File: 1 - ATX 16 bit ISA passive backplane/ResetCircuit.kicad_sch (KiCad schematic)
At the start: 32 parts

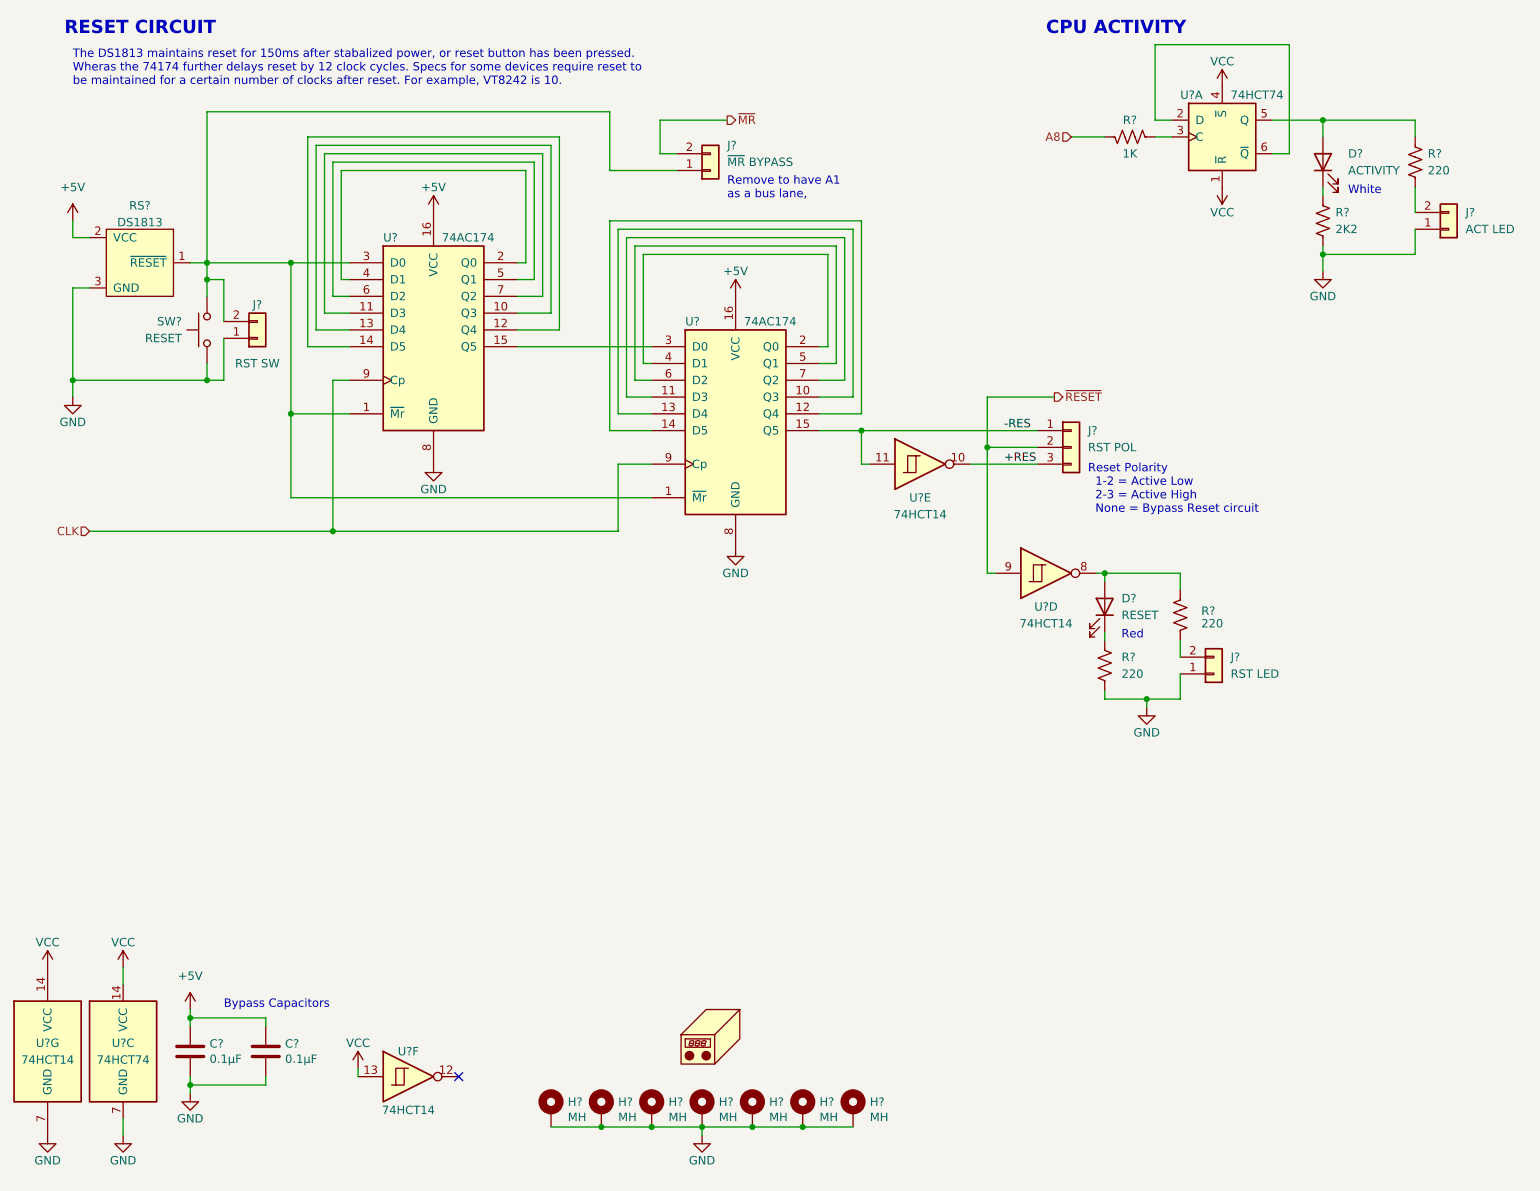
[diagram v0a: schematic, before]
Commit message: Removed unessential components and added capacitors on the bus lanes. Still need work for on the silkscreen side.
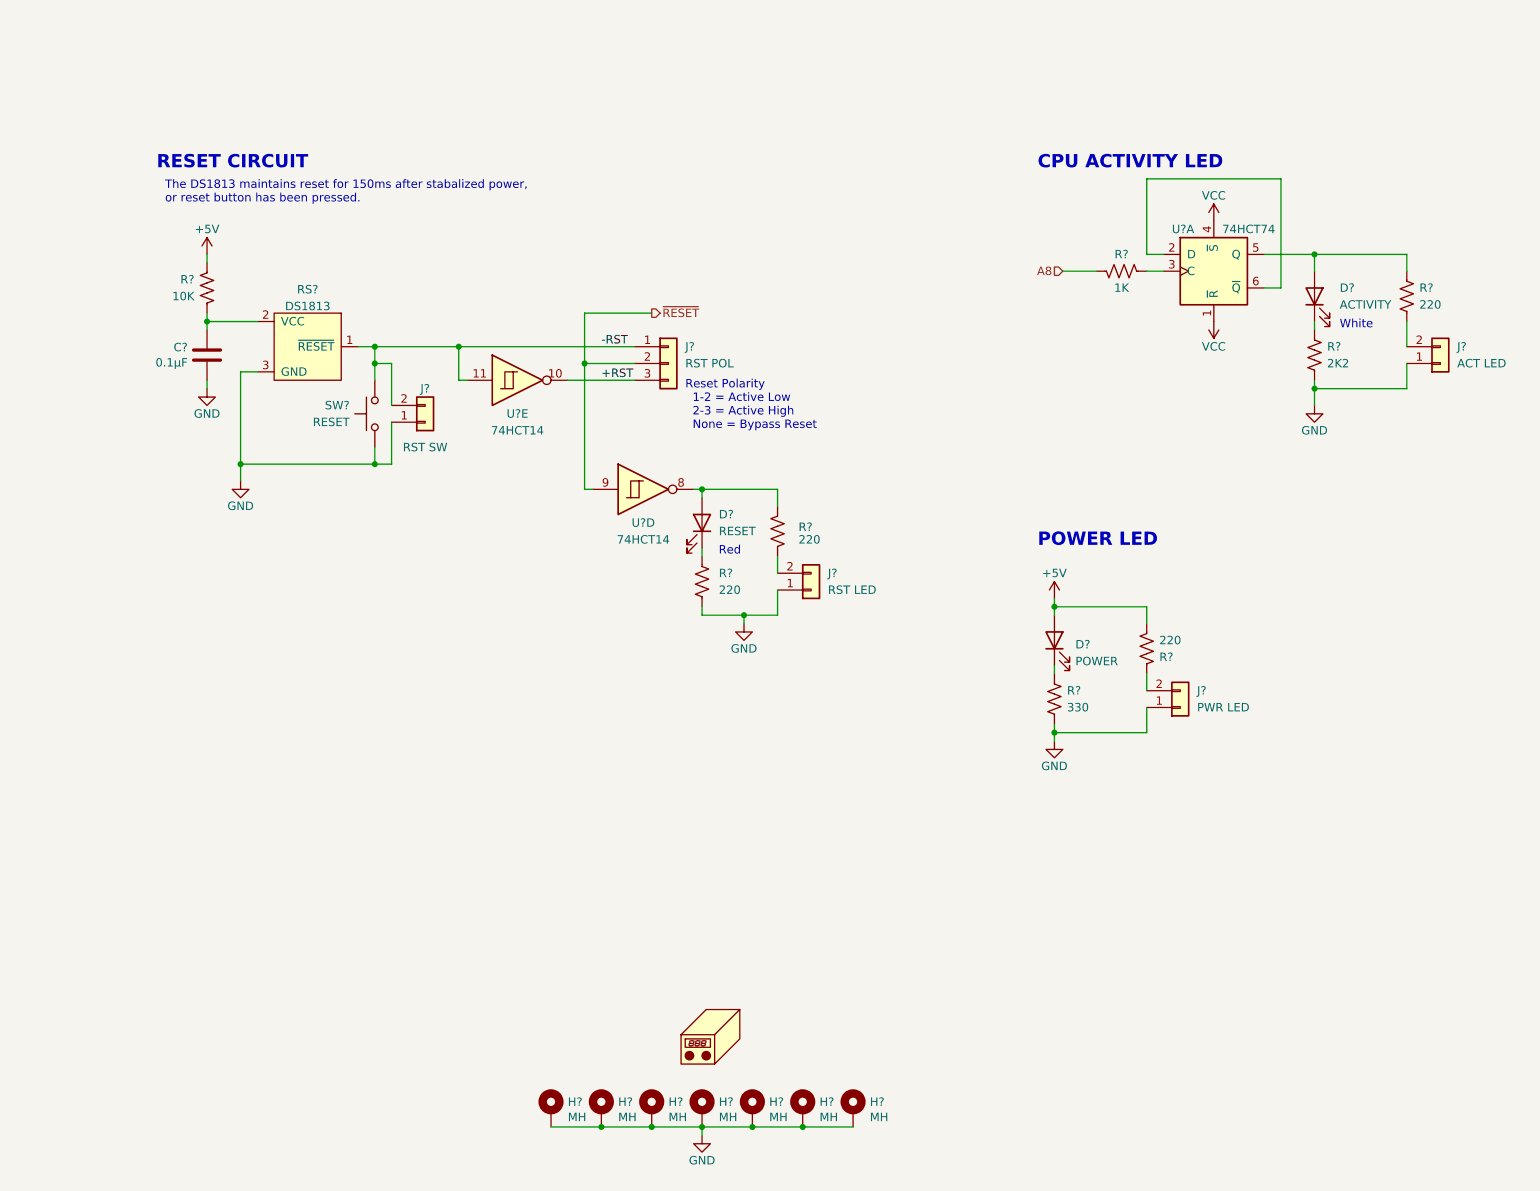
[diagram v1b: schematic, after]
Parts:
- removed C? (x2): 0.1µF, Capacitor_THT:C_Disc_D3.0mm_W1.6mm_P2.50mm, symbol Device:C
- removed J?: ~{MR} BYPASS, Connector_PinHeader_2.54mm:PinHeader_1x02_P2.54mm_Vertical, symbol Connector_Generic:Conn_01x02
- removed U? (x2): 74AC174, Package_DIP:DIP-16_W7.62mm, symbol 74xx:74LS174
- removed U?: 74HCT74, Package_DIP:DIP-14_W7.62mm, symbol 74xx:74HC74
- removed U? (x2): 74HCT14, Package_DIP:DIP-14_W7.62mm, symbol 74xx:74HC14
- added C?: 0.1µF, Capacitor_THT:C_Disc_D3.0mm_W1.6mm_P2.50mm, symbol Device:C
- added D?: POWER, LED_THT:LED_D3.0mm, symbol Device:LED
- added J?: PWR LED, 0 - Library:PinHeader_1x2_Vertical (Modified), symbol Connector_Generic:Conn_01x02
- added R?: 220, Resistor_THT:R_Axial_DIN0207_L6.3mm_D2.5mm_P10.16mm_Horizontal, symbol Device:R_US
- added R?: 330, Resistor_THT:R_Axial_DIN0207_L6.3mm_D2.5mm_P10.16mm_Horizontal, symbol Device:R_US
- added R?: 10K, Resistor_THT:R_Axial_DIN0207_L6.3mm_D2.5mm_P10.16mm_Horizontal, symbol Device:R_US
- J? (x3): footprint Connector_PinHeader_2.54mm:PinHeader_1x02_P2.54mm_Vertical -> 0 - Library:PinHeader_1x2_Vertical (Modified)
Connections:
- net -RES is gone; now on net -RST: J?.1 (Pin_1), U?.11
- net +5V: now also D?.2 (A), R?.1, R?.2; no longer RS?.2 (VCC)
- net GND: now also C?.2, J?.1 (Pin_1), R?.2
- net -RST: now reaches J?.2 (Pin_2), RS?.1 (~{RESET}), SW?.1
- net +RES renamed +RST
- new net: D?.1 (K), R?.1
- new net: J?.2 (Pin_2), R?.1
- new net: C?.1, R?.2, RS?.2 (VCC)
- no-connect marks 1 -> 0
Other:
- note added: "CPU ACTIVITY LED"
- note added: "POWER LED"
- note added: "Reset Polarity 1-2 = Active Low 2-3 = Active High None = Bypass Reset"
- note added: "The DS1813 maintains reset for 150ms after stabalized power, or reset button has been pressed."
- note removed: "Bypass Capacitors"
- note removed: "CPU ACTIVITY"
- note removed: "Remove to have A1 as a bus lane,"
- note removed: "Reset Polarity 1-2 = Active Low 2-3 = Active High None = Bypass Reset circuit"
- note removed: "The DS1813 maintains reset for 150ms after stabalized power, or reset button has been pressed. Wheras the 74174 further delays reset by 12 clock cycles. Specs for some devices require reset to be maintained for a certain number of clocks after reset. For example, VT8242 is 10."
- moved on the sheet: D?, J?, R?, RS?, SW?, U?A, U?D, U?E

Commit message: Minor tweaks to the backplane, and will be sending it out for manufacture
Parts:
- H? (x7): footprint 0 - Library:MountingHole_M3.96_Pad_Via_ATX -> 0_Library:MountingHole_M3.96_Pad_Via_ATX
- J? (x4): footprint 0 - Library:PinHeader_1x2_Vertical (Modified) -> 0_Library:PinHeader_1x2_Vertical (Modified)
- N?: footprint 0 - Library:ATX_Backplane -> 0_Library:ATX_Backplane
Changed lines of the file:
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@@
       (effects (font (size 1.27 1.27)) (justify left))
     )
-    (property "Footprint" "0 - Library:MountingHole_M3.96_Pad_Via_ATX" (at 99.06 189.23 0)
+    (property "Footprint" "0_Library:MountingHole_M3.96_Pad_Via_ATX" (at 99.06 189.23 0)
       (effects (font (size 1.27 1.27)) hide)
     )
@@
       (effects (font (size 1.27 1.27)) (justify left))
     )
-    (property "Footprint" "0 - Library:MountingHole_M3.96_Pad_Via_ATX" (at 121.92 189.23 0)
+    (property "Footprint" "0_Library:MountingHole_M3.96_Pad_Via_ATX" (at 121.92 189.23 0)
       (effects (font (size 1.27 1.27)) hide)
     )
@@
       (effects (font (size 1.27 1.27)) (justify left))
     )
-    (property "Footprint" "0 - Library:PinHeader_1x2_Vertical (Modified)" (at 194.31 128.27 0)
+    (property "Footprint" "0_Library:PinHeader_1x2_Vertical (Modified)" (at 194.31 128.27 0)
       (effects (font (size 1.27 1.27)) hide)
     )
@@
       (effects (font (size 1.27 1.27)) (justify left))
     )
-    (property "Footprint" "0 - Library:MountingHole_M3.96_Pad_Via_ATX" (at 114.3 189.23 0)
+    (property "Footprint" "0_Library:MountingHole_M3.96_Pad_Via_ATX" (at 114.3 189.23 0)
       (effects (font (size 1.27 1.27)) hide)
     )
@@
       (effects (font (size 1.27 1.27)) (justify left))
     )
-    (property "Footprint" "0 - Library:MountingHole_M3.96_Pad_Via_ATX" (at 137.16 189.23 0)
+    (property "Footprint" "0_Library:MountingHole_M3.96_Pad_Via_ATX" (at 137.16 189.23 0)
       (effects (font (size 1.27 1.27)) hide)
     )
@@
       (effects (font (size 1.27 1.27)) (justify left))
     )
-    (property "Footprint" "0 - Library:MountingHole_M3.96_Pad_Via_ATX" (at 129.54 189.23 0)
+    (property "Footprint" "0_Library:MountingHole_M3.96_Pad_Via_ATX" (at 129.54 189.23 0)
       (effects (font (size 1.27 1.27)) hide)
     )
@@
       (effects (font (size 1.27 1.27)) (justify left) hide)
     )
-    (property "Footprint" "0 - Library:ATX_Backplane" (at 125.73 176.53 0)
+    (property "Footprint" "0_Library:ATX_Backplane" (at 125.73 176.53 0)
       (effects (font (size 1.27 1.27)) hide)
     )
@@
       (effects (font (size 1.27 1.27)) (justify left))
     )
-    (property "Footprint" "0 - Library:PinHeader_1x2_Vertical (Modified)" (at 233.68 76.2 0)
+    (property "Footprint" "0_Library:PinHeader_1x2_Vertical (Modified)" (at 233.68 76.2 0)
       (effects (font (size 1.27 1.27)) hide)
     )
@@
       (effects (font (size 1.27 1.27)) (justify left))
     )
-    (property "Footprint" "0 - Library:PinHeader_1x2_Vertical (Modified)" (at 138.43 110.49 0)
+    (property "Footprint" "0_Library:PinHeader_1x2_Vertical (Modified)" (at 138.43 110.49 0)
       (effects (font (size 1.27 1.27)) hide)
     )
@@
       (effects (font (size 1.27 1.27)) (justify left))
     )
-    (property "Footprint" "0 - Library:MountingHole_M3.96_Pad_Via_ATX" (at 144.78 189.23 0)
+    (property "Footprint" "0_Library:MountingHole_M3.96_Pad_Via_ATX" (at 144.78 189.23 0)
       (effects (font (size 1.27 1.27)) hide)
     )
@@
       (effects (font (size 1.27 1.27)))
     )
-    (property "Footprint" "0 - Library:PinHeader_1x2_Vertical (Modified)" (at 80.01 85.09 0)
+    (property "Footprint" "0_Library:PinHeader_1x2_Vertical (Modified)" (at 80.01 85.09 0)
       (effects (font (size 1.27 1.27)) hide)
     )
@@
       (effects (font (size 1.27 1.27)) (justify left))
     )
-    (property "Footprint" "0 - Library:MountingHole_M3.96_Pad_Via_ATX" (at 106.68 189.23 0)
-      (effects (font (size 1.27 1.27)) hide)
-    )
+    (property "Footprint" "0_Library:MountingHole_M3.96_Pad_Via_ATX" (at 106.68 189.23 0)
+      (effects (font (size 1.27 1.27)) hide)
+    )

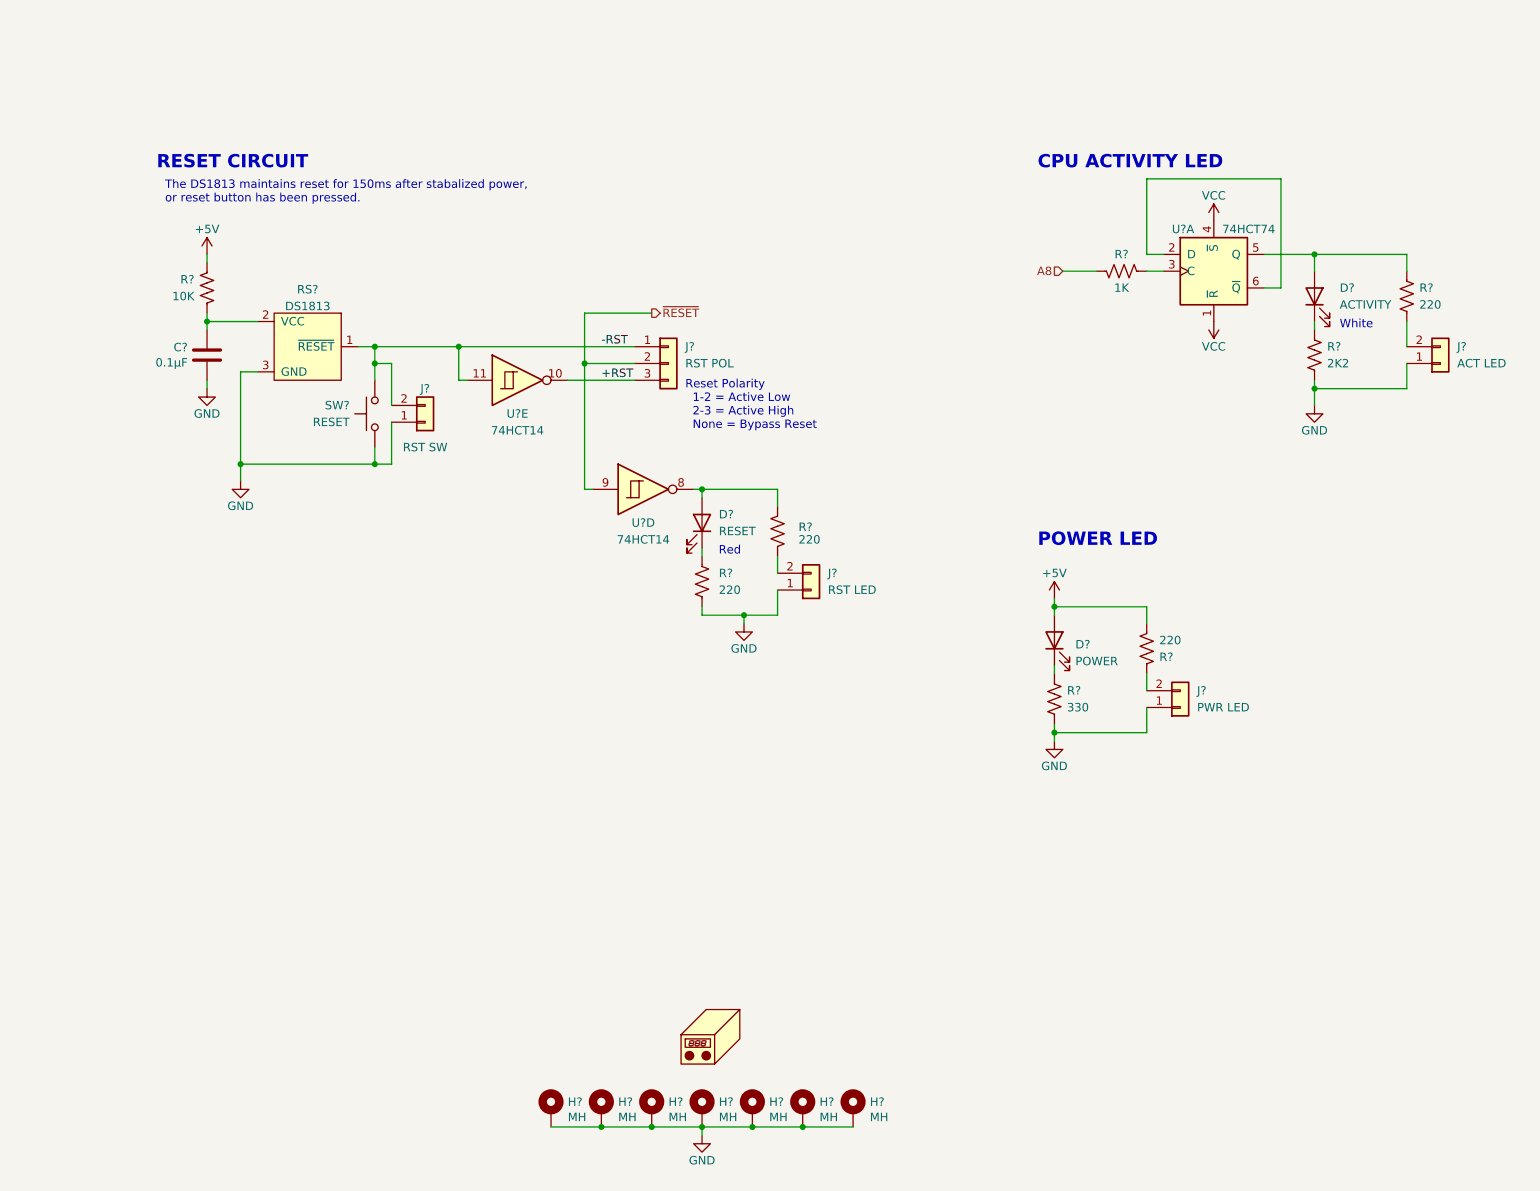
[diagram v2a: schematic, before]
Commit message: Updated disk activity circuit in mother board, and improved layout in CPU card
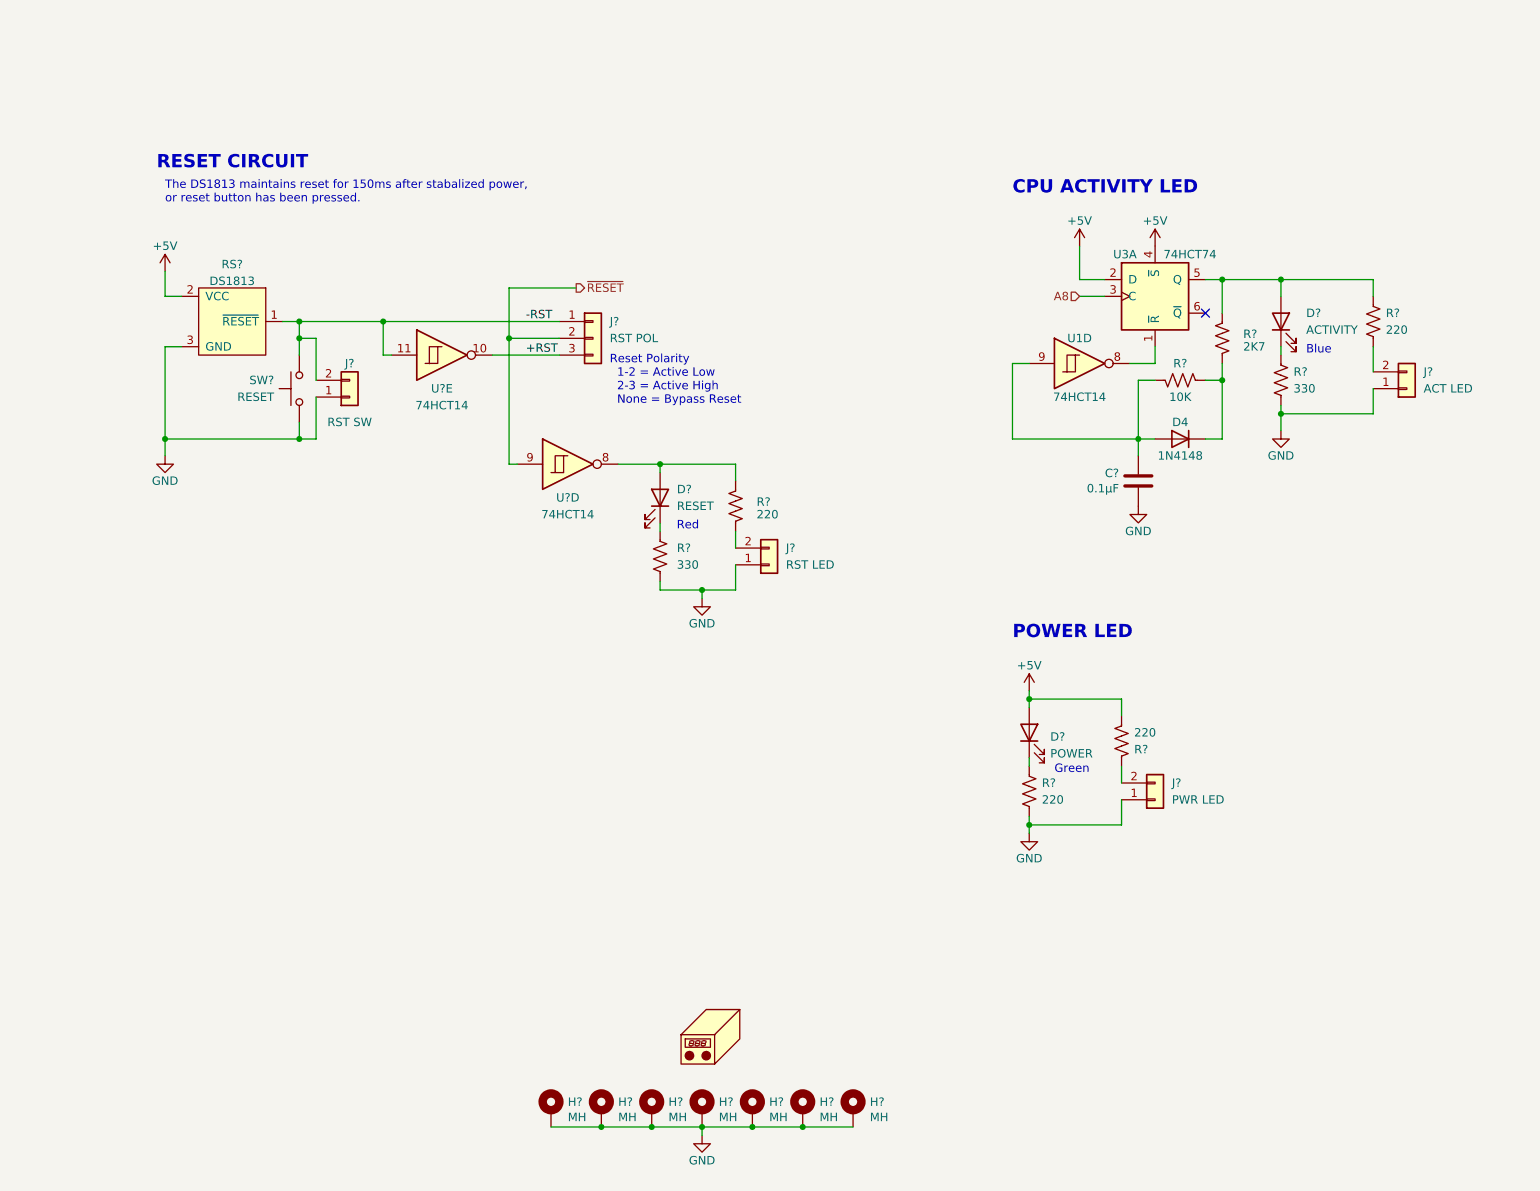
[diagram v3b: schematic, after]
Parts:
- removed C?: 0.1µF, Capacitor_THT:C_Disc_D3.0mm_W1.6mm_P2.50mm, symbol Device:C
- removed R?: 1K, Resistor_THT:R_Axial_DIN0207_L6.3mm_D2.5mm_P10.16mm_Horizontal, symbol Device:R_US
- removed R?: 10K, Resistor_THT:R_Axial_DIN0207_L6.3mm_D2.5mm_P10.16mm_Horizontal, symbol Device:R_US
- removed U?: 74HCT74, Package_DIP:DIP-14_W7.62mm, symbol 74xx:74HC74
- added C?: 0.1µF, Capacitor_THT:C_Disc_D3.0mm_W1.6mm_P2.50mm, symbol Device:C
- added D4: 1N4148, Diode_THT:D_DO-35_SOD27_P7.62mm_Horizontal, symbol Diode:1N4148
- added R?: 2K7, Resistor_THT:R_Axial_DIN0207_L6.3mm_D2.5mm_P10.16mm_Horizontal, symbol Device:R_US
- added R?: 10K, Resistor_THT:R_Axial_DIN0207_L6.3mm_D2.5mm_P10.16mm_Horizontal, symbol Device:R_US
- added U1: 74HCT14, Package_DIP:DIP-14_W7.62mm, symbol 74xx:74HC14
- added U3: 74HCT74, Package_DIP:DIP-14_W7.62mm, symbol 74xx:74HC74
- R?: value 330 -> 220
- R?: value 2K2 -> 330
- R?: value 220 -> 330
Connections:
- net +5V: now also RS?.2 (VCC), U3.2 (D), U3.4 (~{S})
- net A8: now also U3.3 (C)
- net GND: now also C?.2
- net at D?.2 (A), R?.1: now also R?.2, U3.5 (Q)
- new net: U1.8, U3.1 (~{R})
- new net: C?.1, D4.2 (A), R?.2, U1.9
- new net: D4.1 (K), R?.1, R?.1
- no-connect marks 0 -> 1
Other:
- note added: "Blue"
- note added: "Green"
- note removed: "White"
- title: (none) -> Reset and CPU activity circuits
- moved on the sheet: D?, J?, R?, RS?, SW?, U?D, U?E
